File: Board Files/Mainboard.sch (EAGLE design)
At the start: 76 parts

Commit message: Board Updates
-Reset Switch
-Velocity Pot
-Frames
-Started connecting shift registers
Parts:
- removed LED-REGISTER_3, LED_REGISTER_1, LED_REGISTER_2: SN74HC595N, SparkFun-IC-Logic:74HC595N
- added C1: 10uF, SparkFun-Capacitors:10UF-POLAR-RADIAL-2.5MM-25V-20%
- added J1: I2C Display, SparkFun-Connectors:CONN_04
- added LED_REG_1, LED_REG_2, LED_REG_3: SN74HC595N, SparkFun-IC-Logic:74HC595N
- added R25, R26: 10k, SparkFun-Resistors:10KOHM-HORIZ-1/4W-1%
- added S1: MOMENTARY-SWITCH-6MM-SMD, SparkFun-Switches:MOMENTARY-SWITCH-SPST-SMD-6.0X3.5MM
- added VR1: 10k, SparkFun-Resistors:POTENTIOMETER_SLIDE-20MM-1/10W-20%
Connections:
- new net LED_DATA: B1.4, LED_REG_1.SER
- new net N$26: B1.*5
- new net N$27: B1.*6
- new net N$28: B1.7
- new net N$29: B1.8
- new net REG1-2_DATA: LED_REG_1.QH*, LED_REG_2.SER
- new net REG2-3_DATA: LED_REG_2.QH*, LED_REG_3.SER
- new net RESET: B1.RESET, S1.1
- new net SCL: B1.*3, J1.3, R25.1
- new net SDA: B1.2, J1.4, R26.1
- new net VELPOT: B1.*9, VR1.S
- net GND: now also B1.GND, B1.GND@1, C1.-, J1.2, LED_REG_1.GND, LED_REG_2.GND, LED_REG_3.GND, S1.2, VR1.E
- net LED1-1: now also LED_REG_1.QA
- net LED1-2: now also LED_REG_1.QB
- net LED1-3: now also LED_REG_1.QC
- net LED1-4: now also LED_REG_1.QD
- net LED1-5: now also LED_REG_1.QE
- net LED1-6: now also LED_REG_1.QF
- net LED1-7: now also LED_REG_1.QG
- net LED1-8: now also LED_REG_1.QH
- net LED2-1: now also LED_REG_2.QA
- net LED2-2: now also LED_REG_2.QB
- net LED2-3: now also LED_REG_2.QC
- net LED2-4: now also LED_REG_2.QD
- net LED2-5: now also LED_REG_2.QE
- net LED2-6: now also LED_REG_2.QF
- net LED2-7: now also LED_REG_2.QG
- net LED2-8: now also LED_REG_2.QH
- net LED3-1: now also LED_REG_3.QA
- net LED3-2: now also LED_REG_3.QB
- net LED3-3: now also LED_REG_3.QC
- net LED3-4: now also LED_REG_3.QD
- net LED3-5: now also LED_REG_3.QE
- net LED3-6: now also LED_REG_3.QF
- net LED3-7: now also LED_REG_3.QG
- net LED3-8: now also LED_REG_3.QH
- net VCC: now also C1.+, J1.1, LED_REG_1.VCC, LED_REG_2.VCC, LED_REG_3.VCC, R25.2, R26.2, VR1.A
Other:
- note added: "70mA limit for 74HC595's. Use 220-440 ohm resistors w/ Adafruit Super Bright LEDs (2.75V) 220 recommended w/white"
- note added: "Decoupling Cap"
- note added: "I2C Display Header"
- note added: "If you don't have one, that's fine, just jump the pads with a wire."
- note added: "LED Shift Registers"
- note added: "Reset Button"
- note added: "VCC GND SCL SDA"
- note added: "Velocity Potentiometer"

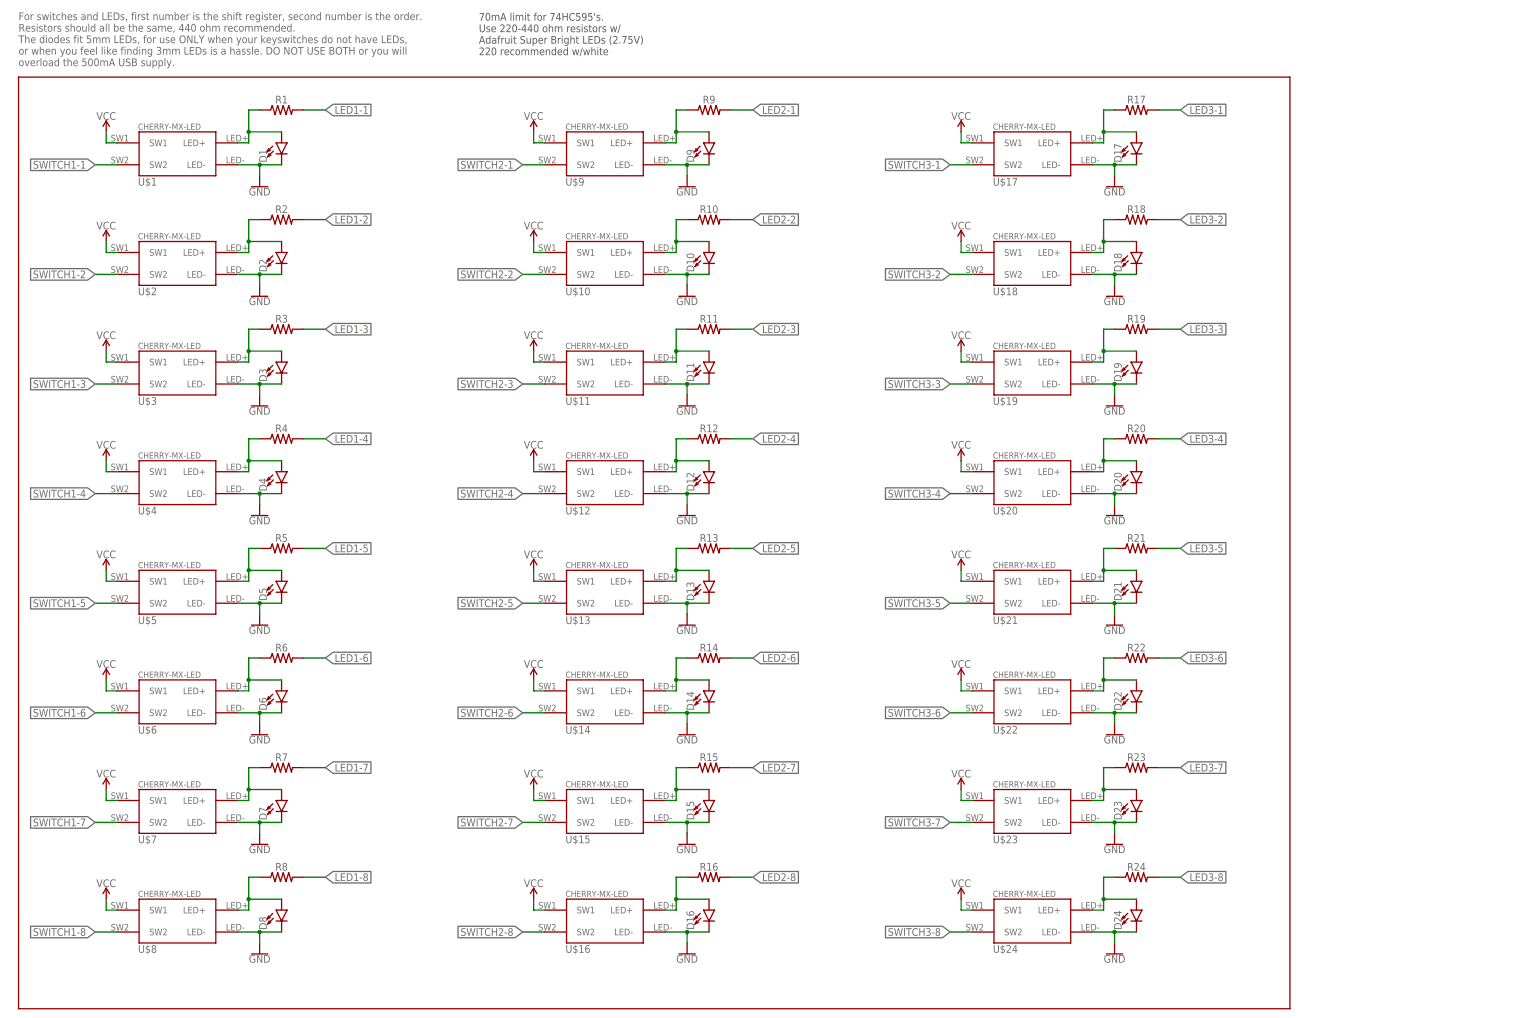
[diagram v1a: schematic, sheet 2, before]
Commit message: Finished Shift Registers
-Finished pins on 595s
-Added and completed pins on 4021B's
-Added 10k resistors to switch side
-Added issues to test and consider to github
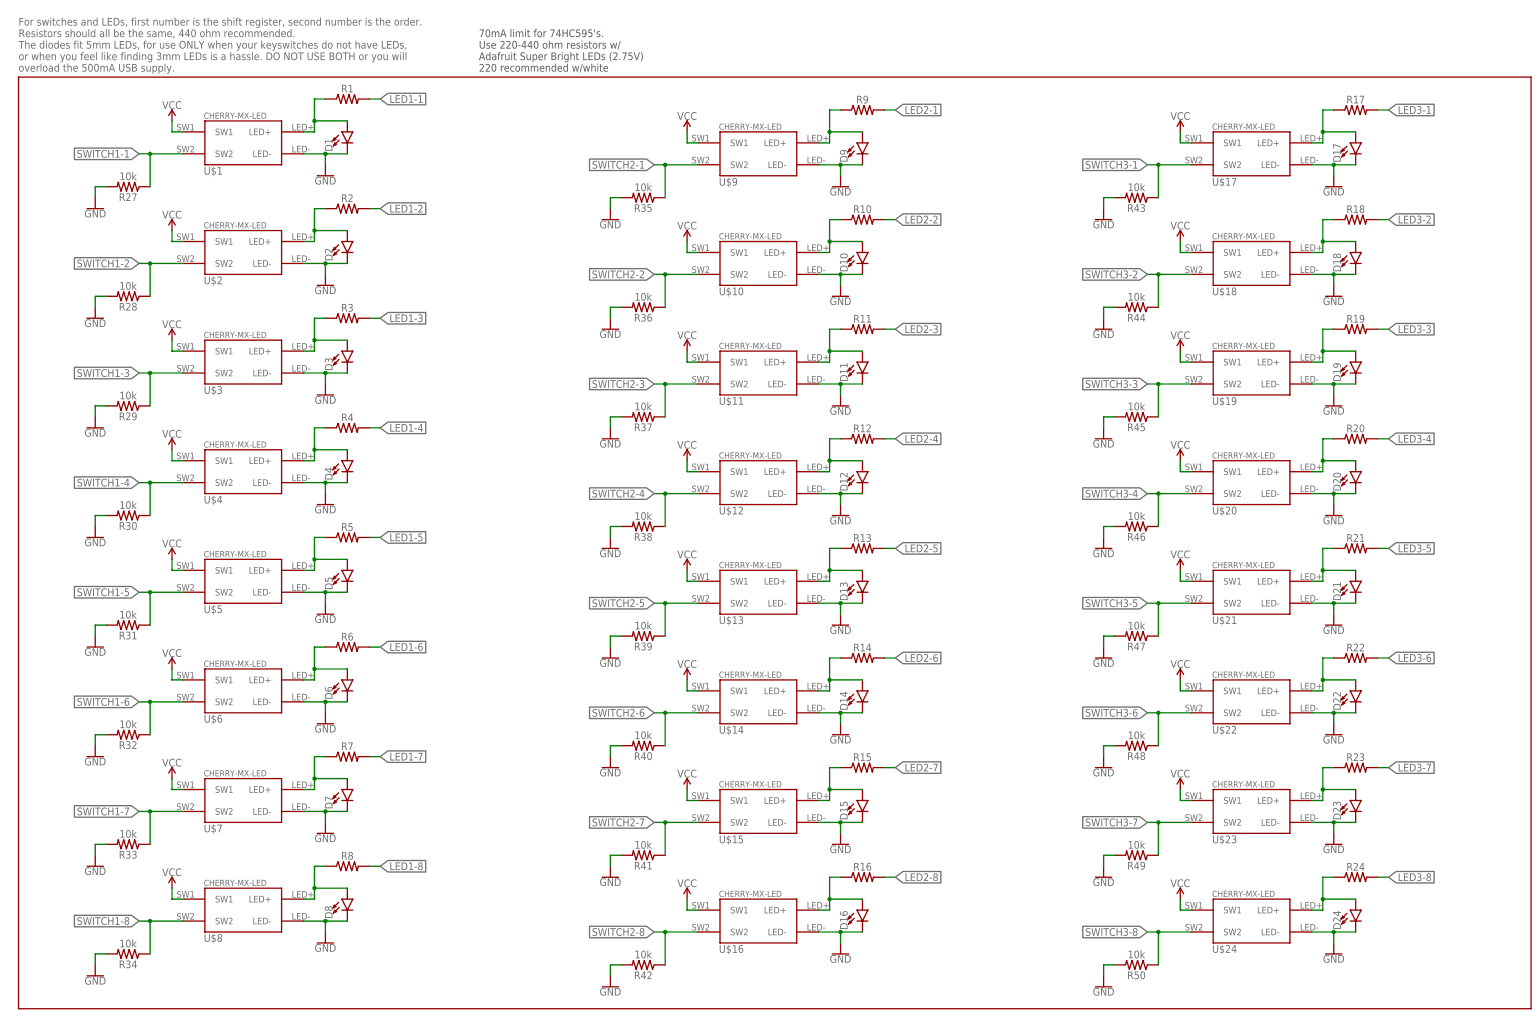
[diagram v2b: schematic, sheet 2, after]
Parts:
- added KEY_REG_1, KEY_REG_2, KEY_REG_3: 4021N, 40xx:4021N
- added R27, R28, R29, R30, R31, R32, R33, R34, R35, R36, R37, R38, R39, R40, R41, R42, R43, R44, R45, R46, R47, R48, R49, R50: 10k, SparkFun-Resistors:10KOHM-HORIZ-1/4W-1%
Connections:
- net REG1-2_DATA renamed LREG1-2_DATA
- net REG2-3_DATA renamed LREG2-3_DATA
- removed net N$26: B1.*5
- removed net N$27: B1.*6
- new net KEY_CLOCK: KEY_REG_1A.CLK, KEY_REG_2A.CLK, KEY_REG_3A.CLK
- new net KEY_DATA: KEY_REG_1A.Q8
- new net KEY_LATCH: KEY_REG_1A.P/!S, KEY_REG_2A.P/!S, KEY_REG_3A.P/!S
- new net KREG2-1_DATA: KEY_REG_1A.SI, KEY_REG_2A.Q8
- new net KREG3-2_DATA: KEY_REG_2A.SI, KEY_REG_3A.Q8
- new net LED_CLOCK: B1.*5, LED_REG_1.SCK, LED_REG_2.SCK, LED_REG_3.SCK
- new net LED_ENABLE: LED_REG_1.G, LED_REG_2.G, LED_REG_3.G
- new net LED_LATCH: B1.*6, LED_REG_1.RCK, LED_REG_2.RCK, LED_REG_3.RCK
- net GND: now also KEY_REG_1P.VSS, KEY_REG_2P.VSS, KEY_REG_3P.VSS, R27.2, R28.2, R29.2, R30.2, R31.2, R32.2, R33.2, R34.2, R35.2, R36.2, R37.2, R38.2, R39.2, R40.2, R41.2, R42.2, R43.2, R44.2, R45.2, R46.2, R47.2, R48.2, R49.2, R50.2
- net SWITCH1-1: now also KEY_REG_1A.P1, R27.1
- net SWITCH1-2: now also KEY_REG_1A.P2, R28.1
- net SWITCH1-3: now also KEY_REG_1A.P3, R29.1
- net SWITCH1-4: now also KEY_REG_1A.P4, R30.1
- net SWITCH1-5: now also KEY_REG_1A.P5, R31.1
- net SWITCH1-6: now also KEY_REG_1A.P6, R32.1
- net SWITCH1-7: now also KEY_REG_1A.P7, R33.1
- net SWITCH1-8: now also KEY_REG_1A.P8, R34.1
- net SWITCH2-1: now also KEY_REG_2A.P1, R35.1
- net SWITCH2-2: now also KEY_REG_2A.P2, R36.1
- net SWITCH2-3: now also KEY_REG_2A.P3, R37.1
- net SWITCH2-4: now also KEY_REG_2A.P4, R38.1
- net SWITCH2-5: now also KEY_REG_2A.P5, R39.1
- net SWITCH2-6: now also KEY_REG_2A.P6, R40.1
- net SWITCH2-7: now also KEY_REG_2A.P7, R41.1
- net SWITCH2-8: now also KEY_REG_2A.P8, R42.1
- net SWITCH3-1: now also KEY_REG_3A.P1, R43.1
- net SWITCH3-2: now also KEY_REG_3A.P2, R44.1
- net SWITCH3-3: now also KEY_REG_3A.P3, R45.1
- net SWITCH3-4: now also KEY_REG_3A.P4, R46.1
- net SWITCH3-5: now also KEY_REG_3A.P5, R47.1
- net SWITCH3-6: now also KEY_REG_3A.P6, R48.1
- net SWITCH3-7: now also KEY_REG_3A.P7, R49.1
- net SWITCH3-8: now also KEY_REG_3A.P8, R50.1
- net VCC: now also KEY_REG_1P.VDD, KEY_REG_2P.VDD, KEY_REG_3P.VDD, LED_REG_1.SCL, LED_REG_2.SCL, LED_REG_3.SCL
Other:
- note added: "If you don't have one, that's fine, just jump the pads with a wire to reset."
- note added: "Switch Shift Registers"
- note removed: "If you don't have one, that's fine, just jump the pads with a wire."
- moved on the sheet: C1, D1, D10, D11, D12, D13, D14, D15, D16, D17, D18, D19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
